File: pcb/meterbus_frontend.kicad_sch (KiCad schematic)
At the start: 38 parts, among them Q2 AO3400A, U10 AMS1117-5.0, U2 SN74HC132DR, U3 ISO6721RBDR

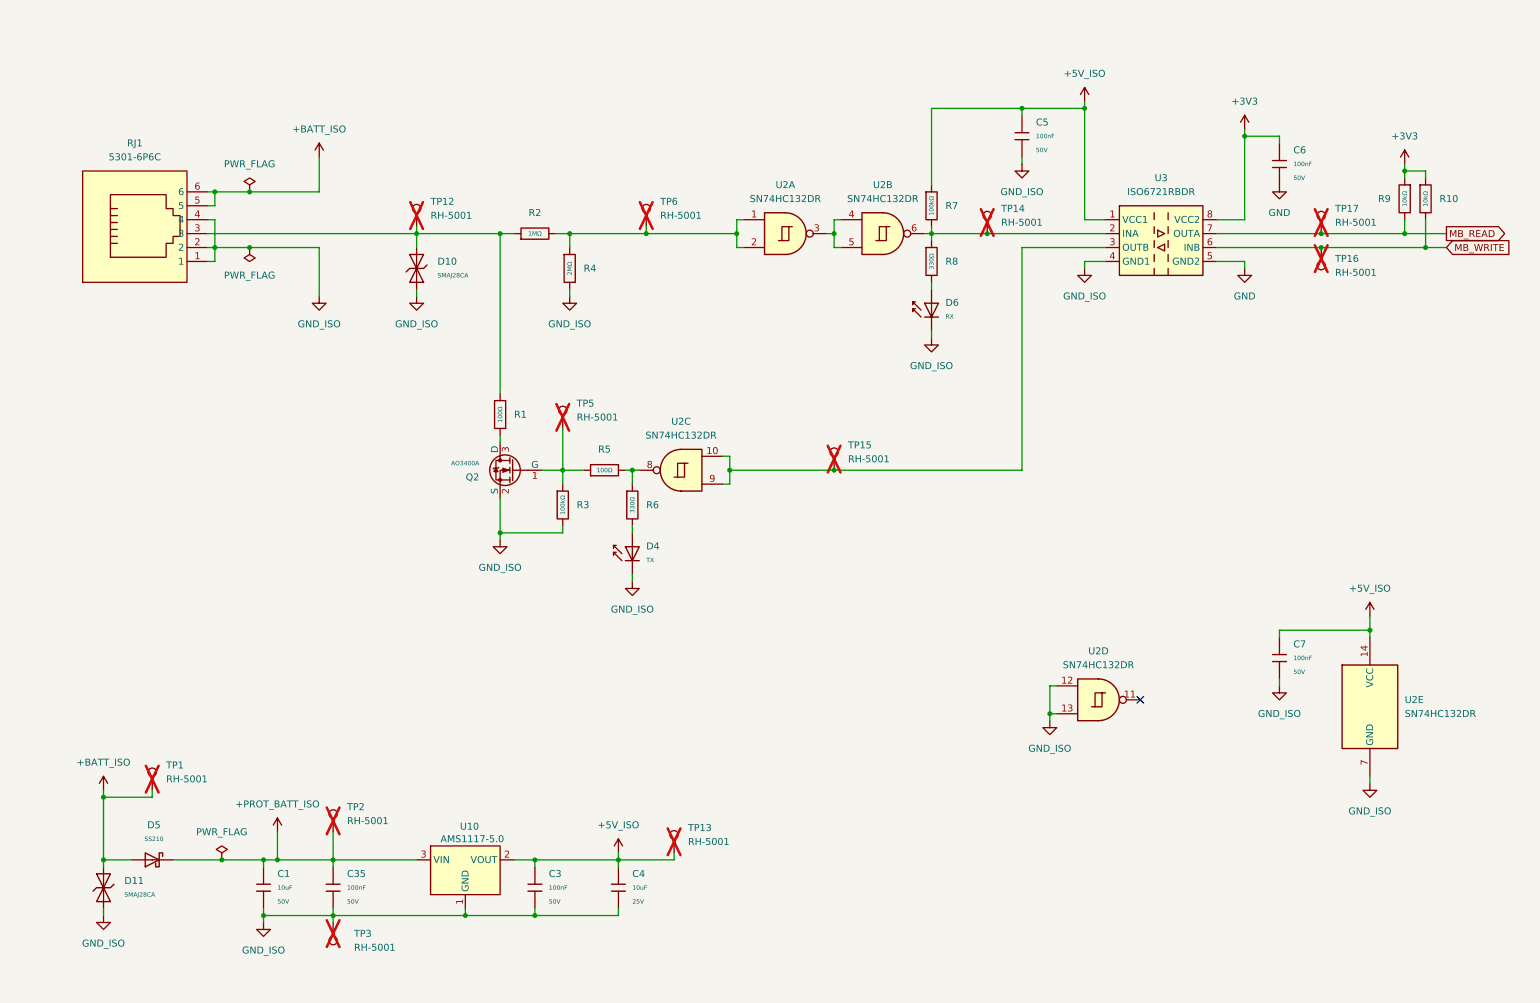
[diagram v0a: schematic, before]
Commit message: sch: replace mcu and clean up schematic
Fixes #27
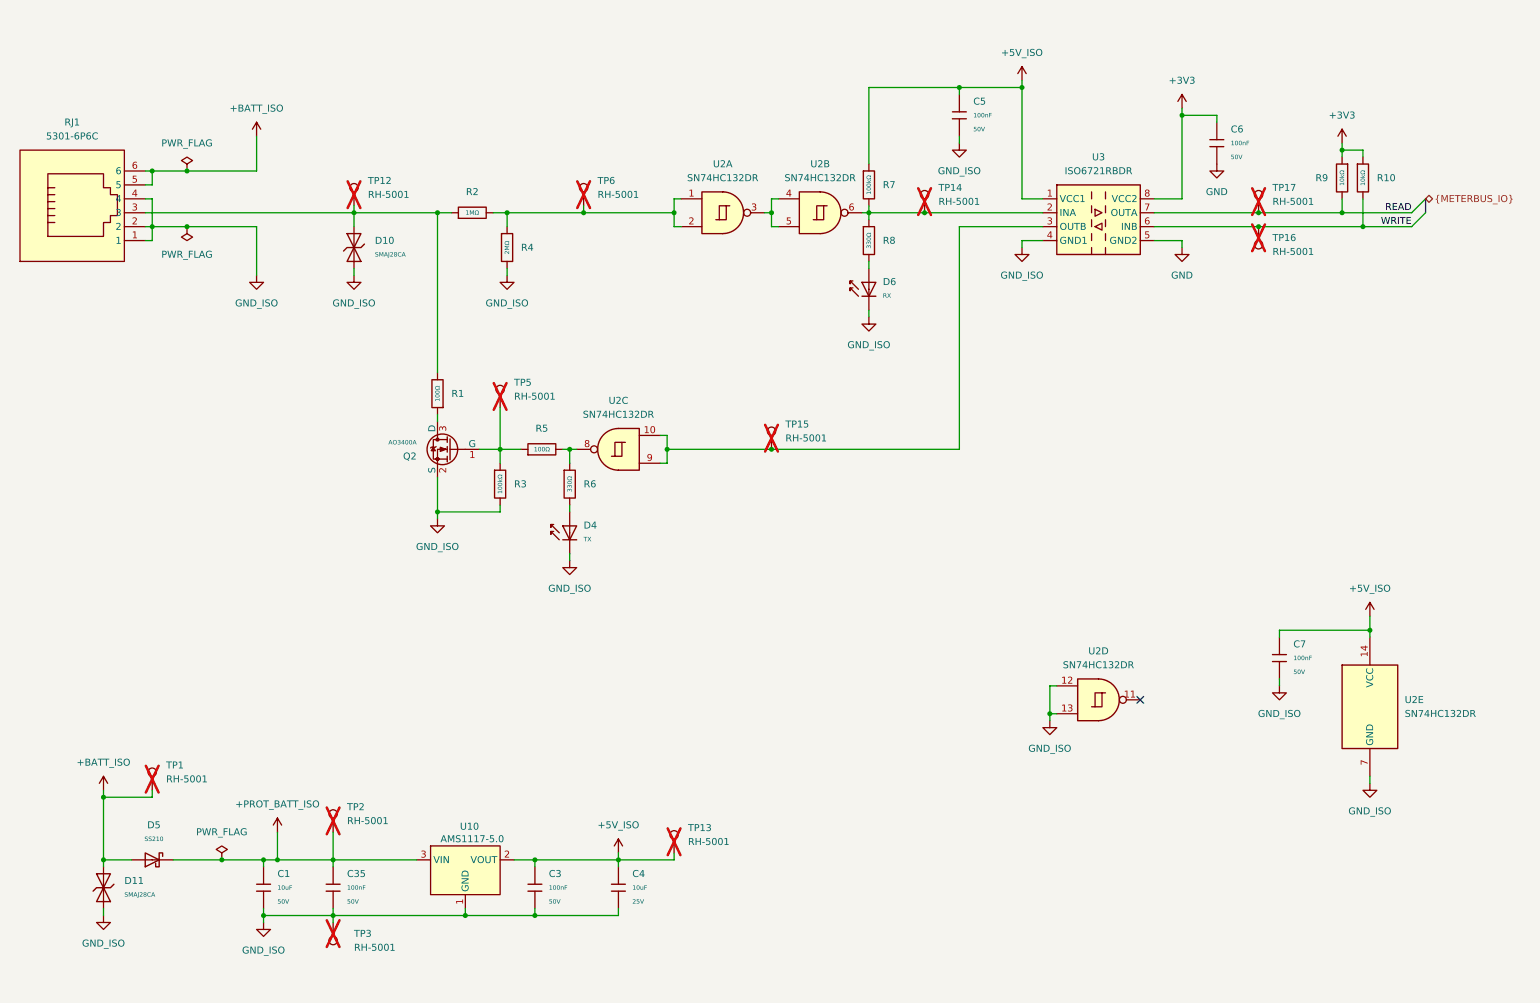
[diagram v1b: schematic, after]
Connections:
- net MB_READ renamed READ
- net MB_WRITE renamed WRITE
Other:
- moved on the sheet: C5, C6, D10, D4, D6, Q2, R1, R10, R2, R3, R4, R5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

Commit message: sch: replace green led resistor
Fixes #6
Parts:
- removed R8: 330Ω, PCM_JLCPCB:R_0603, symbol PCM_JLCPCB-Resistors:0603,330Ω
- added R8: 2.2kΩ, PCM_JLCPCB:R_0603, symbol PCM_JLCPCB-Resistors:0603,2.2kΩ
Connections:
- net at R7.2, TP14.1, U2.6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: now also R8.1
- net at D6.2: now also R8.2

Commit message: sch: replace meterbus led resistors again
Fixes #46
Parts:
- removed R6: 330Ω, PCM_JLCPCB:R_0603, symbol PCM_JLCPCB-Resistors:0603,330Ω
- removed R8: 2.2kΩ, PCM_JLCPCB:R_0603, symbol PCM_JLCPCB-Resistors:0603,2.2kΩ
- added R6: 2.7kΩ, PCM_JLCPCB:R_0603, symbol PCM_JLCPCB-Resistors:0603,2.7kΩ
- added R8: 10kΩ, PCM_JLCPCB:R_0603, symbol PCM_JLCPCB-Resistors:0603,10kΩ
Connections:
- net at R5.2, U2.8: now also R6.1
- net at D4.2: now also R6.2
- net at R7.2, TP14.1, U2.6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: now also R8.1
- net at D6.2: now also R8.2

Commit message: sch: remove ineffective meterbus pullup resistor
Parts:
- removed R7: 100kΩ, PCM_JLCPCB:R_0603, symbol PCM_JLCPCB-Resistors:0603,100kΩ

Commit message: sch: switch to vertical meterbus jack
Replace the original right-angled RJ11 meterbus connector with a vertical one to make routing and placement easier. Relates to #42
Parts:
- removed RJ1: 5301-6P6C, EasyEDA:RJ45-TH_5301-6P6C, symbol EasyEDA:5301-6P6C
- added RJ2: 5201-6P6C, EasyEDA:RJ45-TH_RRCH-5201-6P6C, symbol EasyEDA:5201-6P6C
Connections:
- net +BATT_ISO: now also RJ2.5, RJ2.6
- net GND_ISO: now also RJ2.1, RJ2.2, RJ2.4
- net at D10.2, R1.2, R2.1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: now also RJ2.3

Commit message: sch: replace meterbus psu
Replaces the AMS1117-5 regulator with a HT7533 3.3v regulator which has
a much wider input range, allowing for more appropriate TVS diode
protection.

Also rejigs some test points.

Relates to #48
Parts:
- removed D11: SMAJ28CA, PCM_JLCPCB:D_DO-214AC(SMA), symbol PCM_JLCPCB-Diodes:TVS-Bi,SMAJ28CA
- removed R6: 2.7kΩ, PCM_JLCPCB:R_0603, symbol PCM_JLCPCB-Resistors:0603,2.7kΩ
- removed R8: 10kΩ, PCM_JLCPCB:R_0603, symbol PCM_JLCPCB-Resistors:0603,10kΩ
- removed TP1, TP13, TP2, TP3: RH-5001, EasyEDA:TEST-TH_BD2.54-P1.4_BLACK, symbol Connector:TestPoint
- removed U10: AMS1117-5.0, EasyEDA:SOT-223_L6.5-W3.5-P2.30-LS7.0-BR, symbol EasyEDA:AMS1117-5.0
- added D3: SMBJ17CA, EasyEDA:SMB_L4.3-W3.6-LS5.4-BI, symbol EasyEDA:SMBJ17CA_C3720411
- added TP21: 3V3_ISO, TestPoint:TestPoint_Pad_D1.0mm, symbol Connector:TestPoint_Square
- added TP25: GND_ISO, TestPoint:TestPoint_Plated_Hole_D2.0mm, symbol Connector:TestPoint_Square
- added TP26: BATT_ISO, TestPoint:TestPoint_Plated_Hole_D2.0mm, symbol Connector:TestPoint_Square
- added U1: HT7533, PCM_JLCPCB:SOT-89-3_L4.5-W2.5-P1.50-LS4.2-BR, symbol PCM_JLCPCB-Power:LDO, 3.3V, 0.1A
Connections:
- net +5V_ISO: no longer C3.1, C4.1
- net +BATT_ISO: now also D3.2 (A), TP26.1
- net GND_ISO: now also D3.1 (K), TP25.1, U1.1 (GND)
- net +PROT_BATT_ISO: no longer names the net of C1.1, C35.1, D5.1
- net +PROT_BATT_ISO: now also U1.2 (VIN)
- new net +3V3_ISO: C3.1, C4.1, TP21.1, U1.3 (VOUT)
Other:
- note added: "3.3V supply"
- note added: "Test Points"
- moved on the sheet: C1, C3, C35, C4, D5

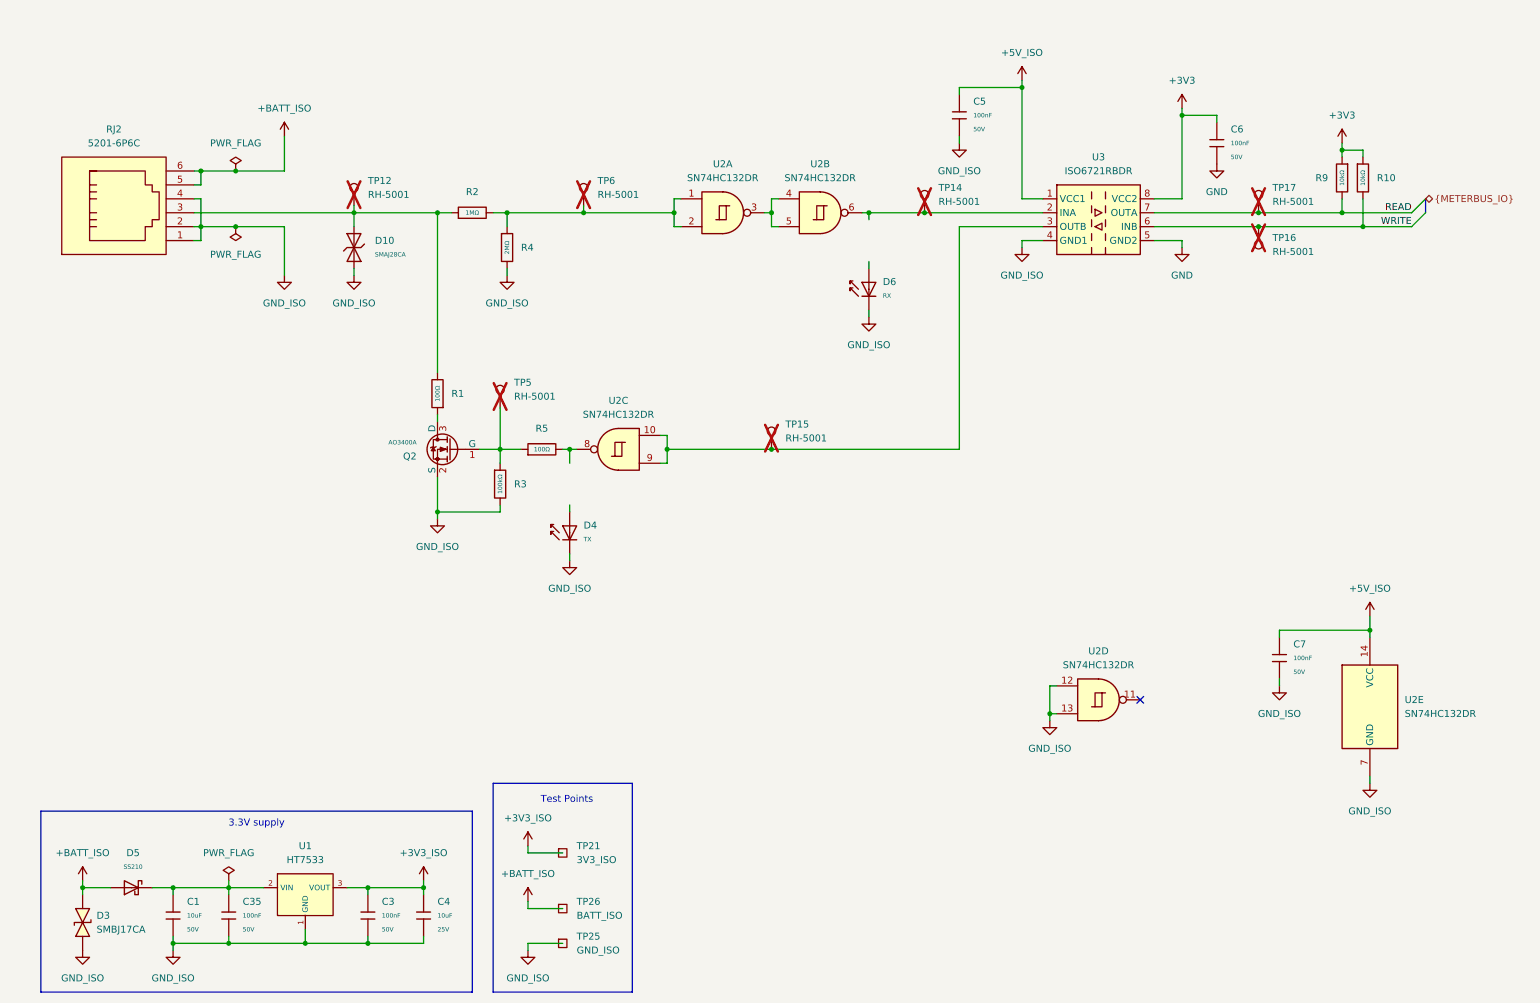
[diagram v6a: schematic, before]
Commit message: sch: update meterbus frontend
Fixes #48

This is a complete rework of the Meterbus frontend, including power
supply IC replacement, gate IC replacement, ESD protection adjustments,
LED resistor adjustments, and general schematic cleanup.

The other major change is the removal of the bus input voltage divider,
which has been replaced with a series limiter and a clamping design
using the internal clamp diodes of the HC14 (Explicitly supported by
Nexperia)
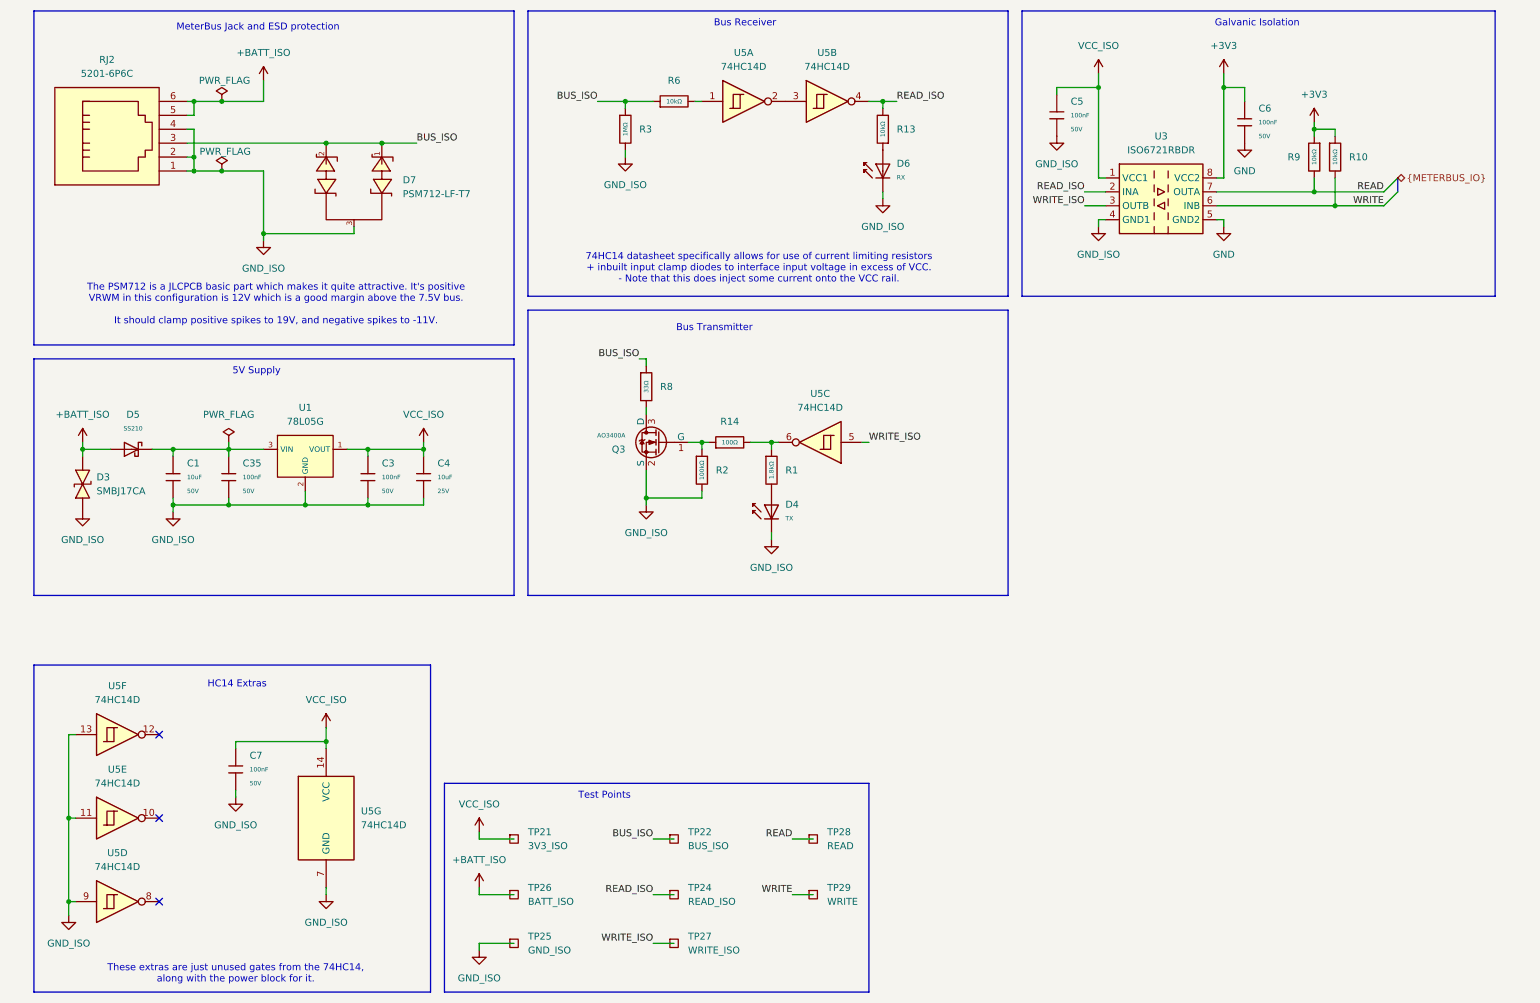
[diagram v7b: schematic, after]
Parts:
- removed D10: SMAJ28CA, PCM_JLCPCB:D_DO-214AC(SMA), symbol PCM_JLCPCB-Diodes:TVS-Bi,SMAJ28CA
- removed Q2: AO3400A, PCM_JLCPCB:Q_SOT-23, symbol PCM_JLCPCB-Transistors:NMOS,AO3400A
- removed R1, R5: 100Ω, PCM_JLCPCB:R_0603, symbol PCM_JLCPCB-Resistors:0603,100Ω
- removed R2: 1MΩ, PCM_JLCPCB:R_0603, symbol PCM_JLCPCB-Resistors:0603,1MΩ
- removed R3: 100kΩ, PCM_JLCPCB:R_0603, symbol PCM_JLCPCB-Resistors:0603,100kΩ
- removed R4: 2MΩ, PCM_JLCPCB:R_0603, symbol PCM_JLCPCB-Resistors:0603,2MΩ
- removed TP12, TP14, TP15, TP16, TP17, TP5, TP6: RH-5001, EasyEDA:TEST-TH_BD2.54-P1.4_BLACK, symbol Connector:TestPoint
- removed U1: HT7533, PCM_JLCPCB:SOT-89-3_L4.5-W2.5-P1.50-LS4.2-BR, symbol PCM_JLCPCB-Power:LDO, 3.3V, 0.1A
- removed U2: SN74HC132DR, EasyEDA:SOIC-14_L8.7-W3.9-P1.27-LS6.0-BL, symbol custom_symbols:74HC132
- added D7: PSM712-LF-T7, PCM_JLCPCB:SOT-23-3_L3.0-W1.7-P0.95-LS2.9-BR, symbol PCM_JLCPCB-Diode-Packages:TVS-Bi, PSM712-LF-T7
- added Q3: AO3400A, PCM_JLCPCB:Q_SOT-23, symbol PCM_JLCPCB-Transistors:NMOS,AO3400A
- added R1: 1.8kΩ, PCM_JLCPCB:R_0603, symbol PCM_JLCPCB-Resistors:0603,1.8kΩ
- added R13, R6: 10kΩ, PCM_JLCPCB:R_0603, symbol PCM_JLCPCB-Resistors:0603,10kΩ
- added R14: 100Ω, PCM_JLCPCB:R_0603, symbol PCM_JLCPCB-Resistors:0603,100Ω
- added R2: 100kΩ, PCM_JLCPCB:R_0603, symbol PCM_JLCPCB-Resistors:0603,100kΩ
- added R3: 1MΩ, PCM_JLCPCB:R_0603, symbol PCM_JLCPCB-Resistors:0603,1MΩ
- added R8: 33Ω, PCM_JLCPCB:R_0603, symbol PCM_JLCPCB-Resistors:0603,33Ω
- added TP22: BUS_ISO, TestPoint:TestPoint_Pad_D1.0mm, symbol Connector:TestPoint_Square
- added TP24: READ_ISO, TestPoint:TestPoint_Pad_D1.0mm, symbol Connector:TestPoint_Square
- added TP27: WRITE_ISO, TestPoint:TestPoint_Pad_D1.0mm, symbol Connector:TestPoint_Square
- added TP28: READ, TestPoint:TestPoint_Pad_D1.0mm, symbol Connector:TestPoint_Square
- added TP29: WRITE, TestPoint:TestPoint_Pad_D1.0mm, symbol Connector:TestPoint_Square
- added U1: 78L05G, PCM_JLCPCB:SOT-89-3_L4.5-W2.5-P1.50-LS4.2-BR, symbol PCM_JLCPCB-Power:LDO, 5V, 0.1A
- added U5: 74HC14D, PCM_JLCPCB:SOIC-14_L8.7-W3.9-P1.27-LS6.0-BL, symbol custom_symbols:74HC14
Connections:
- net +5V_ISO is gone; now on net VCC_ISO: C5.1, C7.1, U3.1 (VCC1)
- net GND_ISO: now also D7.3 (K), Q3.2 (S), R2.2, R3.2, U1.2 (GND), U5.11, U5.13, U5.7 (GND), U5.9
- net READ: now also TP28.1
- net WRITE: now also TP29.1
- net BUS_ISO: now reaches RJ2.3
- net BUS_ISO: now also D7.1 (A1), D7.2 (A1), R3.1, R6.1, R8.1, TP22.1
- net WRITE_ISO: now reaches U3.3 (OUTB)
- net WRITE_ISO: now also TP27.1, U5.5
- net READ_ISO: now reaches U3.2 (INA)
- net READ_ISO: now also R13.2, TP24.1, U5.4
- net at C1.1, C35.1, D5.1: now also U1.3 (VIN)
- net at D4.2: now also R1.2
- net at D6.2: now also R13.1
- net +3V3_ISO renamed VCC_ISO
- net VCC_ISO: now also U1.1 (VOUT), U5.14 (VCC)
- new net: Q3.1 (G), R14.1, R2.1
- new net: R1.1, R14.2, U5.6
- new net: Q3.3 (D), R8.2
- new net: R6.2, U5.1
- new net: U5.2, U5.3
- no-connect marks 1 -> 3
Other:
- note added: "5V Supply"
- note added: "74HC14 datasheet specifically allows for use of current limiting resistors + inbuilt input clamp diodes to interface input voltage in excess of VCC. - Note that this does inject some current onto the VCC rail."
- note added: "Bus Receiver"
- note added: "Bus Transmitter"
- note added: "Galvanic Isolation"
- note added: "HC14 Extras"
- note added: "MeterBus Jack and ESD protection"
- note added: "The PSM712 is a JLCPCB basic part which makes it quite attractive. It's positive VRWM in this configuration is 12V which is a good margin above the 7.5V bus. It should clamp positive spikes to 19V, and negative spikes to -11V."
- note added: "These extras are just unused gates from the 74HC14, along with the power block for it."
- note removed: "3.3V supply"
- moved on the sheet: C1, C3, C35, C4, C5, C6, C7, D3, D4, D5, D6, R10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
